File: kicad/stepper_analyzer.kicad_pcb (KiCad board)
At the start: 2 copper layers, 102 x 57 mm, 23 parts, among them J1 Connector_Conn_01x04_Male, J2 Connector_Conn_01x04_Male, M1 Motor, Q1 AO3400A, U1 ACS70331EOLCTR-2P5B3, U2 ACS70331EOLCTR-2P5B3, U3 Pico

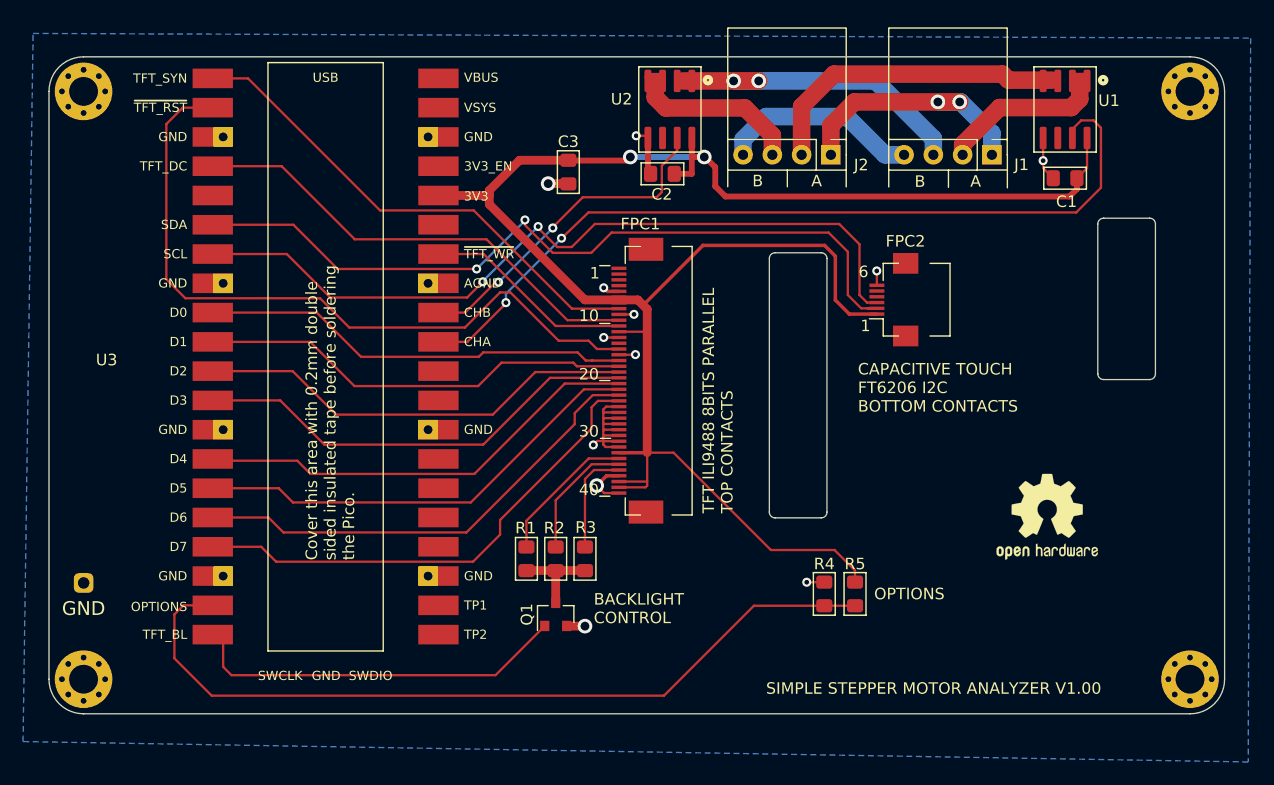
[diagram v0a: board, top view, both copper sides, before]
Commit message: update to current kicad model (for CC6920BSO)
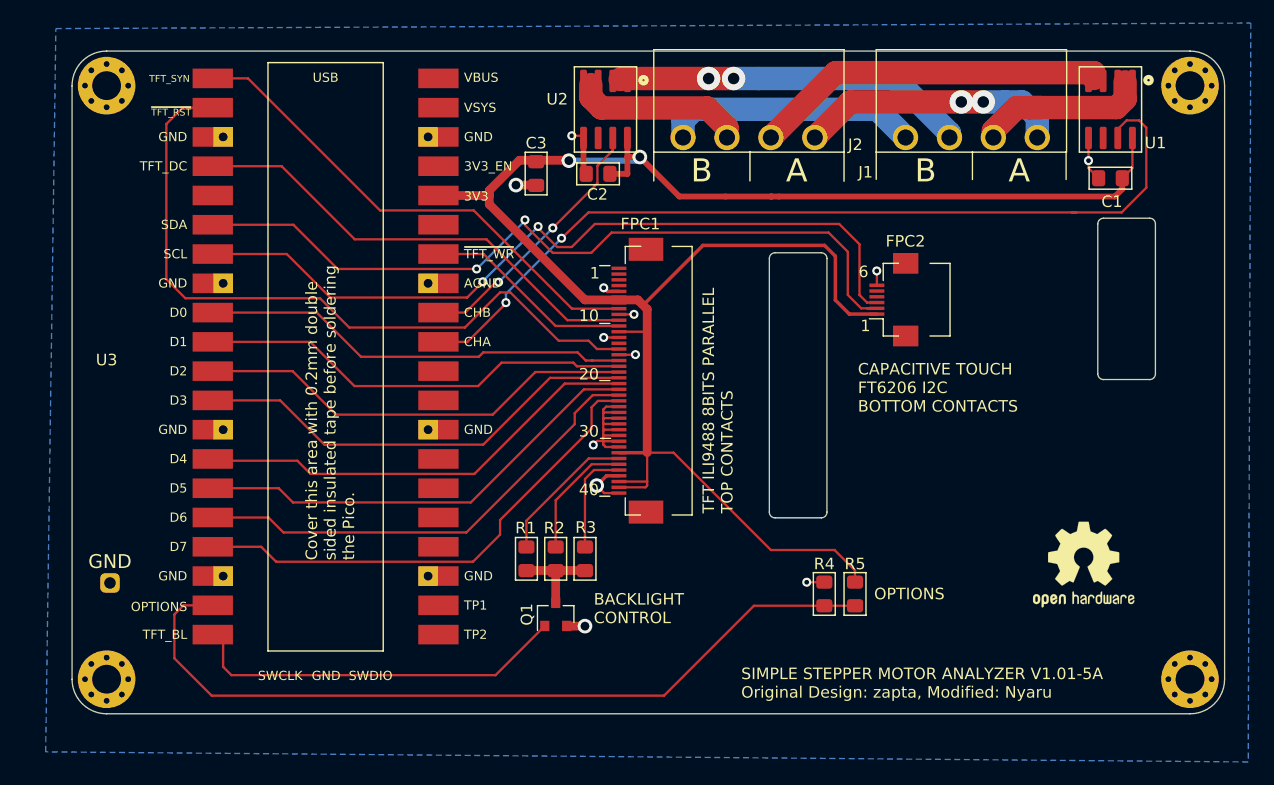
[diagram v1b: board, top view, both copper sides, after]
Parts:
- J1, J2: footprint stepper_motor_analyzer:connector_4pins_horizontal -> Connector:Connector_green_big
- moved C2 5.59 mm to (46.6, -46.8)
- moved U2 5.59 mm to (47.3, -52.4)
- moved LOGO1 5.21 mm to (88.8, -13.0)
- moved J1 4.21 mm to (84.7, -50.0)
- moved C1 3.94 mm to (91.1, -46.5)
- moved U1 3.94 mm to (91.1, -52.4)
- moved C3 2.80 mm to (41.3, -46.9)
- moved TP3 2.29 mm to (4.29, -11.4)
- moved H2 2.06 mm to (4.00, -54.5)
- moved J2 2.05 mm to (65.4, -50.0)
- moved H1 2.00 mm to (4.00, -3.00)
- moved H3 0.50 mm to (98.0, -54.5)
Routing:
- net +3V3: track 165.2 -> 173.3 mm
- net /CHB: track 29.9 -> 23.9 mm
- net Net-(J1-Pad4): track 17.5 -> 22.2 mm
- net /CHA: track 73.4 -> 77.7 mm
- net Net-(J2-Pad2): track 27.4 -> 30.9 mm
- net Net-(J1-Pad3): track 27.4 -> 30.6 mm
- net Net-(J1-Pad1): track 22.2 -> 22.9 mm
- net Net-(J1-Pad2): track 15.1 -> 15.7 mm
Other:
- board size 102 x 57 mm -> 100 x 57.5 mm
- board text added: "SIMPLE STEPPER MOTOR ANALYZER V1.01-5A Original Design: zapta, Modified: Nyaru"
- board text removed: "SIMPLE STEPPER MOTOR ANALYZER V1.00"
